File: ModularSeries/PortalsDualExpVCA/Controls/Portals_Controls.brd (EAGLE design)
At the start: 48.5 x 98 mm, 15 parts, among them SW1 SPDT_SWITCHDW1, SW2 SPDT_SWITCHDW1

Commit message: DRC check fixes on Prism, Portals, TimeSeeds and Knives
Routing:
- net AGND: track 142.0 -> 141.3 mm
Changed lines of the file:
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@@
 <wire x1="33" y1="56.7" x2="33.02" y2="57.785" width="0.6096" layer="1"/>
 <wire x1="33.02" y1="57.785" x2="33" y2="65.3" width="0.6096" layer="1" curve="2.417014"/>
-<wire x1="33" y1="65.3" x2="33.02" y2="66.04" width="0.6096" layer="1"/>
 <contactref element="R2" pad="LUGR"/>
 <wire x1="33" y1="65.3" x2="33.02" y2="66.675" width="0.6096" layer="1"/>

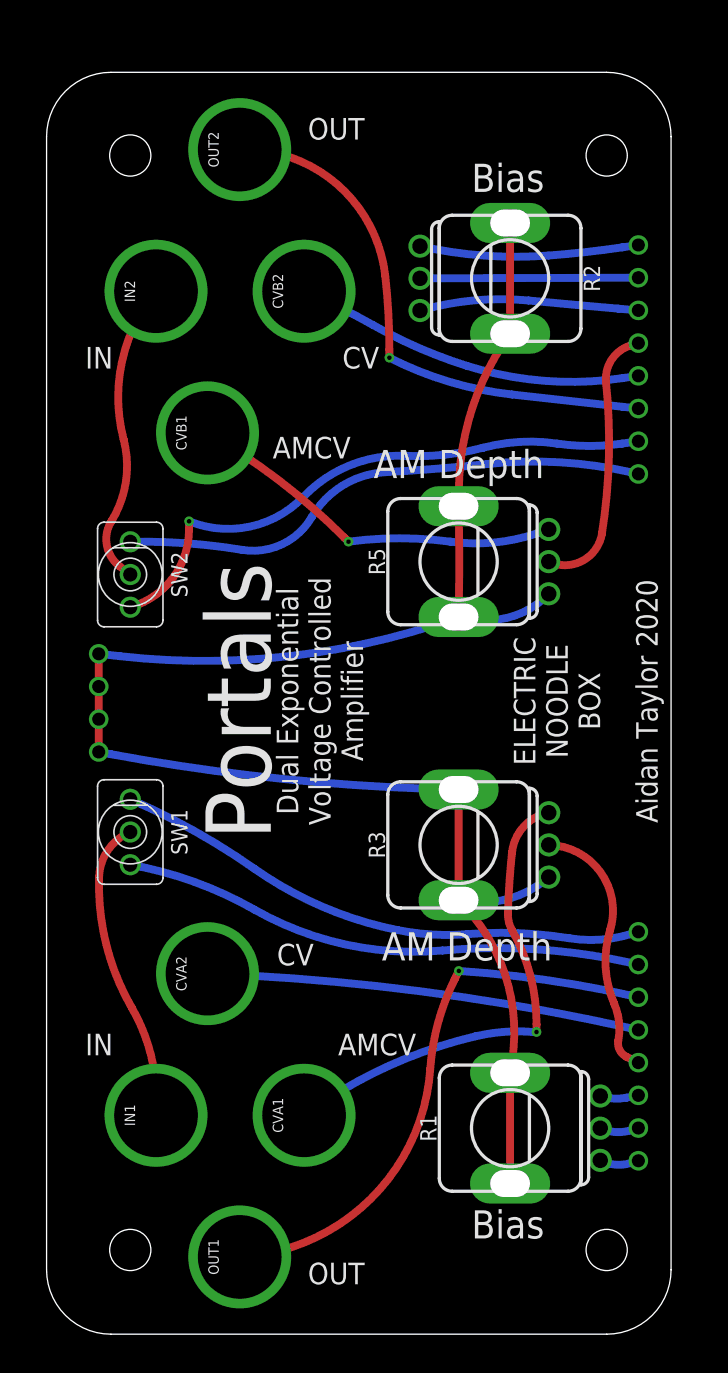
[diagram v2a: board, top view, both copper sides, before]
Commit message: Pulse output fixed on Knives, schematics and layout updated. Panel added for Portals
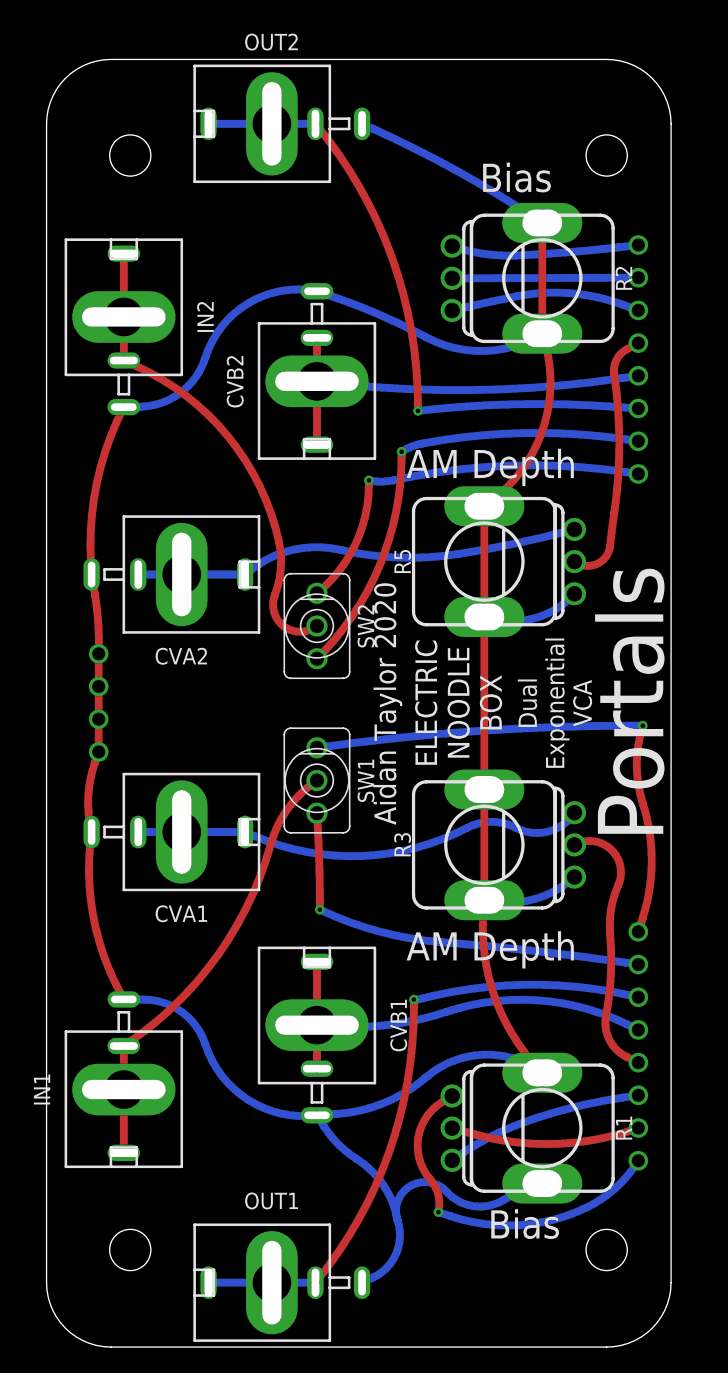
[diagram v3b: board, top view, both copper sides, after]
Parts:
- CVA1, CVA2, CVB1, CVB2, IN1, IN2, OUT1, OUT2: value BANANA_PANEL -> COMBI-JACKCINCHNANA; device ElectricNoodleBox:BANANA_PANEL -> ElectricNoodleBox:NEWCOMBOJACK_PANEL
- moved CVB1 46.8 mm to (22.0, 25.0)
- moved CVA2 31.1 mm to (11.5, 60.0), turned to 270 degrees
- moved CVA1 24.0 mm to (11.5, 40.0), turned to 270 degrees
- moved SW1 15.0 mm to (22.0, 44.0)
- moved SW2 15.0 mm to (22.0, 56.0)
- moved CVB2 7.07 mm to (22.0, 75.0), turned to 180 degrees
- moved IN1 3.20 mm to (7.00, 20.0), turned to 180 degrees
- moved IN2 3.20 mm to (7.00, 80.0)
- moved OUT1 3.20 mm to (18.5, 5.00), turned to 90 degrees
- moved OUT2 3.20 mm to (18.5, 95.0), turned to 90 degrees
- moved R1 2.50 mm to (39.5, 17.0), turned to 270 degrees
- moved R2 2.50 mm to (39.5, 83.0)
- moved R3 2.00 mm to (35.0, 39.0)
- moved R5 2.00 mm to (35.0, 61.0)
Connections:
- net AGND: now also CVA1.S, CVA2.S, CVB1.S, CVB2.S, IN1.S, IN2.S, OUT1.S, OUT2.S
- net N$1: now also CVB1.CONN, CVB1.T1, CVB1.T2; no longer CVA2.CONN
- net N$11: now also CVA2.CONN, CVA2.T1, CVA2.T2; no longer CVB1.CONN
- net N$19: now also OUT2.T1, OUT2.T2
- net N$2: now also CVB2.T1, CVB2.T2
- net N$22: now also IN2.T1, IN2.T2
- net N$3: now also CVA1.T1, CVA1.T2
- net N$8: now also OUT1.T1, OUT1.T2
- net N$9: now also IN1.T1, IN1.T2
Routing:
- net AGND: track 141.3 -> 244.9 mm
- net N$6: track 3.00 -> 26.6 mm, vias 0 -> 1
- net N$7: track 2.98 -> 15.4 mm
- net N$22: track 22.8 -> 35.1 mm
- net N$5: track 2.99 -> 14.5 mm
- net N$9: track 23.3 -> 33.8 mm
- net N$21: track 41.1 -> 30.6 mm, vias 0 -> 1
- net N$20: track 44.0 -> 35.9 mm
- net N$19: track 41.1 -> 49.1 mm
- net N$10: track 40.5 -> 32.7 mm, vias 0 -> 1
- net N$8: track 42.8 -> 49.1 mm
- net N$2: track 27.3 -> 33.3 mm
- net N$11: track 29.5 -> 34.4 mm, vias 1 -> 0
- net N$3: track 37.9 -> 34.1 mm, vias 1 -> 0
- net N$16: track 17.0 -> 14.5 mm
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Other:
- board size 48.5 x 98 mm -> 48.5 x 100 mm
- board text added: "Dual Exponential VCA"
- board text removed: "AMCV"
- board text removed: "CV"
- board text removed: "Dual Exponential Voltage Controlled Amplifier"
- board text removed: "IN"
- board text removed: "OUT"

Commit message: Panel for TimeSeeds added. TLHP core PCB added
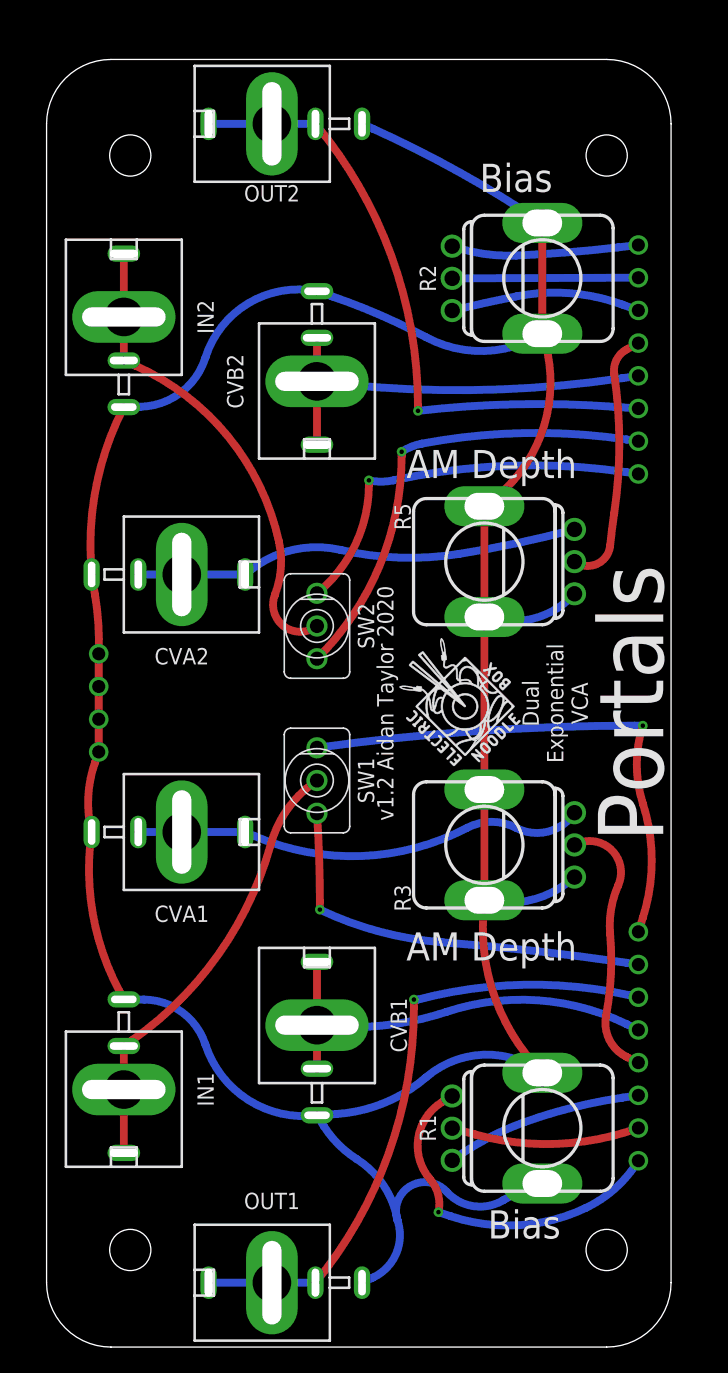
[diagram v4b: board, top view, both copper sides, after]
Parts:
- added U$1, U$2: (no value), ElectricNoodleBox:LOGO10X10
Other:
- board text added: "v1.2 Aidan Taylor 2020"
- board text removed: "Aidan Taylor 2020"
- board text removed: "ELECTRIC NOODLE BOX"
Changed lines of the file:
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@@
 <?xml version="1.0" encoding="utf-8"?>
 <!DOCTYPE eagle SYSTEM "eagle.dtd">
-<eagle version="9.6.0">
+<eagle version="9.6.2">
 <drawing>
 <settings>
@@
 <layer number="17" name="Pads" color="2" fill="1" visible="yes" active="yes"/>
 <layer number="18" name="Vias" color="2" fill="1" visible="yes" active="yes"/>
-<layer number="19" name="Unrouted" color="6" fill="1" visible="yes" active="yes"/>
+<layer number="19" name="Unrouted" color="6" fill="1" visible="no" active="yes"/>
 <layer number="20" name="Dimension" color="24" fill="1" visible="yes" active="yes"/>
 <layer number="21" name="tPlace" color="7" fill="1" visible="yes" active="yes"/>
 <layer number="22" name="bPlace" color="7" fill="1" visible="yes" active="yes"/>
-<layer number="23" name="tOrigins" color="15" fill="1" visible="yes" active="yes"/>
-<layer number="24" name="bOrigins" color="15" fill="1" visible="yes" active="yes"/>
+<layer number="23" name="tOrigins" color="15" fill="1" visible="no" active="yes"/>
+<layer number="24" name="bOrigins" color="15" fill="1" visible="no" active="yes"/>
 <layer number="25" name="tNames" color="7" fill="1" visible="yes" active="yes"/>
-<layer number="26" name="bNames" color="7" fill="1" visible="yes" active="yes"/>
+<layer number="26" name="bNames" color="7" fill="1" visible="no" active="yes"/>
 <layer number="27" name="tValues" color="7" fill="1" visible="no" active="yes"/>
 <layer number="28" name="bValues" color="7" fill="1" visible="no" active="yes"/>
@@
 <layer number="37" name="tTest" color="7" fill="1" visible="no" active="yes"/>
 <layer number="38" name="bTest" color="7" fill="1" visible="no" active="yes"/>
-<layer number="39" name="tKeepout" color="4" fill="11" visible="yes" active="yes"/>
-<layer number="40" name="bKeepout" color="1" fill="11" visible="yes" active="yes"/>
-<layer number="41" name="tRestrict" color="4" fill="10" visible="yes" active="yes"/>
-<layer number="42" name="bRestrict" color="1" fill="10" visible="yes" active="yes"/>
-<layer number="43" name="vRestrict" color="2" fill="10" visible="yes" active="yes"/>
+<layer number="39" name="tKeepout" color="4" fill="11" visible="no" active="yes"/>
+<layer number="40" name="bKeepout" color="1" fill="11" visible="no" active="yes"/>
+<layer number="41" name="tRestrict" color="4" fill="10" visible="no" active="yes"/>
+<layer number="42" name="bRestrict" color="1" fill="10" visible="no" active="yes"/>
+<layer number="43" name="vRestrict" color="2" fill="10" visible="no" active="yes"/>
 <layer number="44" name="Drills" color="7" fill="1" visible="no" active="yes"/>
 <layer number="45" name="Holes" color="7" fill="1" visible="no" active="yes"/>
-<layer number="46" name="Milling" color="3" fill="1" visible="no" active="yes"/>
+<layer number="46" name="Milling" color="3" fill="1" visible="yes" active="yes"/>
 <layer number="47" name="Measures" color="7" fill="1" visible="no" active="yes"/>
-<layer number="48" name="Document" color="7" fill="1" visible="yes" active="yes"/>
+<layer number="48" name="Document" color="7" fill="1" visible="no" active="yes"/>
 <layer number="49" name="Reference" color="7" fill="1" visible="yes" active="yes"/>
 <layer number="50" name="dxf" color="7" fill="1" visible="no" active="no"/>
-<layer number="51" name="tDocu" color="7" fill="1" visible="yes" active="yes"/>
-<layer number="52" name="bDocu" color="7" fill="1" visible="yes" active="yes"/>
+<layer number="51" name="tDocu" color="7" fill="1" visible="no" active="yes"/>
+<layer number="52" name="bDocu" color="7" fill="1" visible="no" active="yes"/>
 <layer number="53" name="tGND_GNDA" color="7" fill="9" visible="no" active="no"/>
 <layer number="54" name="bGND_GNDA" color="1" fill="9" visible="no" active="no"/>
@@
 </layers>
 <board>
-<fusionsync huburn="a.cGVyc29uYWw6dWUyYjdlNGE0" projecturn="a.cGVyc29uYWw6dWUyYjdlNGE0IzIwMjAwNDA1MjgzMzA0MTgx" f3durn="urn:adsk.wipprod:dm.lineage:XfjEGdqqSi-9eQBJwCMZSQ" pcbguid="25871f84-74d5-4f7c-8471-5e8c6ea129c0" lastpulledtime="" lastsyncedchangeguid="" latestrevisionid="99b6558b-c879-43a6-8e26-3714c5e8d2b9" lastsyncedrevisionid="99b6558b-c879-43a6-8e26-3714c5e8d2b9" lastboardhashguid="6312c004-2ac3-f14a-2101-901f34501693" lastpushedtime="2020-05-26T18:30:07Z" linktopcb3d="%12"/>
+<fusionsync huburn="a.cGVyc29uYWw6dWUyYjdlNGE0" projecturn="a.cGVyc29uYWw6dWUyYjdlNGE0IzIwMjAwNDA1MjgzMzA0MTgx" f3durn="urn:adsk.wipprod:dm.lineage:XfjEGdqqSi-9eQBJwCMZSQ" pcbguid="" lastpulledtime="" lastsyncedchangeguid="" latestrevisionid="d212331a-2d97-479f-80fb-10bf9934a00b" lastsyncedrevisionid="d212331a-2d97-479f-80fb-10bf9934a00b" lastboardhashguid="82df6d0b-af90-7169-ef29-52b558667a44" lastpushedtime="2020-06-25T11:09:44Z" linktopcb3d="true"/>
 <plain>
 <text x="37.465" y="90.805" size="2.1844" layer="21" font="vector" ratio="16" align="center">Bias</text>
@@
 <text x="38.1" y="9.525" size="2.1844" layer="21" font="vector" ratio="16" align="center">Bias</text>
 <text x="46.355" y="50" size="5.08" layer="21" font="vector" ratio="16" rot="R90" align="center">Portals</text>
-<text x="40.5" y="50" size="1.4224" layer="21" font="vector" ratio="16" rot="R90" align="center">Dual
+<text x="40.5" y="50" size="1.27" layer="21" font="vector" ratio="16" rot="R90" align="center">Dual
 Exponential
 VCA</text>
-<text x="33" y="50" size="1.6764" layer="21" font="vector" ratio="16" rot="R90" align="center">ELECTRIC
-NOODLE
-BOX</text>
-<text x="27.305" y="50" size="1.6764" layer="21" font="vector" ratio="16" rot="R90" align="center">Aidan Taylor 2020</text>
+<text x="27.305" y="50" size="1.27" layer="21" font="vector" ratio="16" rot="R90" align="center">v1.2 Aidan Taylor 2020</text>
 <wire x1="0" y1="-14.25" x2="50.5" y2="-14.25" width="0.6096" layer="49"/>
 <wire x1="50.5" y1="-14.25" x2="50.5" y2="-8.25" width="0.6096" layer="49"/>
@@
 <element name="BOARD1" library="ElectricNoodleBox" package="PORTALS" value="PORTALS_LINK" x="49.5" y="2.54" smashed="yes" rot="MR0"/>
 <element name="R1" library="ElectricNoodleBox" package="ALPHA_RV09_9MMPOT" value="100K" x="39.5" y="17" smashed="yes" rot="R270">
-<attribute name="NAME" x="45.85" y="17" size="1.27" layer="25" rot="R270" align="center"/>
+<attribute name="NAME" x="30.61" y="17" size="1.27" layer="25" rot="R270" align="center"/>
 <attribute name="VALUE" x="31.88" y="9.38" size="1.27" layer="27" rot="R270" align="center"/>
 </element>
 <element name="R2" library="ElectricNoodleBox" package="ALPHA_RV09_9MMPOT" value="100K" x="39.5" y="83" smashed="yes" rot="R270">
-<attribute name="NAME" x="45.85" y="83" size="1.27" layer="25" rot="R270" align="center"/>
+<attribute name="NAME" x="30.61" y="83" size="1.27" layer="25" rot="R270" align="center"/>
 <attribute name="VALUE" x="31.88" y="75.38" size="1.27" layer="27" rot="R270" align="center"/>
 </element>
 <element name="R3" library="ElectricNoodleBox" package="ALPHA_RV09_9MMPOT" value="100k" x="35" y="39" smashed="yes" rot="R90">
-<attribute name="NAME" x="28.65" y="39" size="1.27" layer="25" rot="R90" align="center"/>
+<attribute name="NAME" x="28.65" y="34.8725" size="1.27" layer="25" rot="R90" align="center"/>
 <attribute name="VALUE" x="42.62" y="46.62" size="1.27" layer="27" rot="R90" align="center"/>
 </element>
 <element name="R5" library="ElectricNoodleBox" package="ALPHA_RV09_9MMPOT" value="100K" x="35" y="61" smashed="yes" rot="R90">
-<attribute name="NAME" x="28.65" y="61" size="1.27" layer="25" rot="R90" align="center"/>
+<attribute name="NAME" x="28.65" y="64.4925" size="1.27" layer="25" rot="R90" align="center"/>
 <attribute name="VALUE" x="42.62" y="68.62" size="1.27" layer="27" rot="R90" align="center"/>
 </element>
@@
 </element>
 <element name="IN1" library="ElectricNoodleBox" package="NEWCOMBOJACK_PANEL" value="COMBI-JACKCINCHNANA" x="7" y="20" smashed="yes" rot="R180">
-<attribute name="NAME" x="0.65" y="20" size="1.27" layer="25" font="vector" rot="R270" align="center"/>
+<attribute name="NAME" x="13.35" y="20" size="1.27" layer="25" font="vector" rot="R270" align="center"/>
 </element>
 <element name="OUT2" library="ElectricNoodleBox" package="NEWCOMBOJACK_PANEL" value="COMBI-JACKCINCHNANA" x="18.5" y="95" smashed="yes" rot="R90">
-<attribute name="NAME" x="18.5" y="101.35" size="1.27" layer="25" font="vector" rot="R180" align="center"/>
+<attribute name="NAME" x="18.5" y="89.6025" size="1.27" layer="25" font="vector" rot="R180" align="center"/>
 </element>
 <element name="IN2" library="ElectricNoodleBox" package="NEWCOMBOJACK_PANEL" value="COMBI-JACKCINCHNANA" x="7" y="80" smashed="yes">
 <attribute name="NAME" x="13.35" y="80" size="1.27" layer="25" font="vector" rot="R90" align="center"/>
 </element>
+<element name="U$1" library="ElectricNoodleBox" package="LOGO10X10" value="" x="38.1" y="45.085" smashed="yes" rot="R90"/>
+<element name="U$2" library="ElectricNoodleBox" package="LOGO10X10" value="" x="33.9725" y="53.6575" smashed="yes" rot="MR270"/>
 </elements>
 <signals>

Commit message: Layout and schematic renders for LHP added
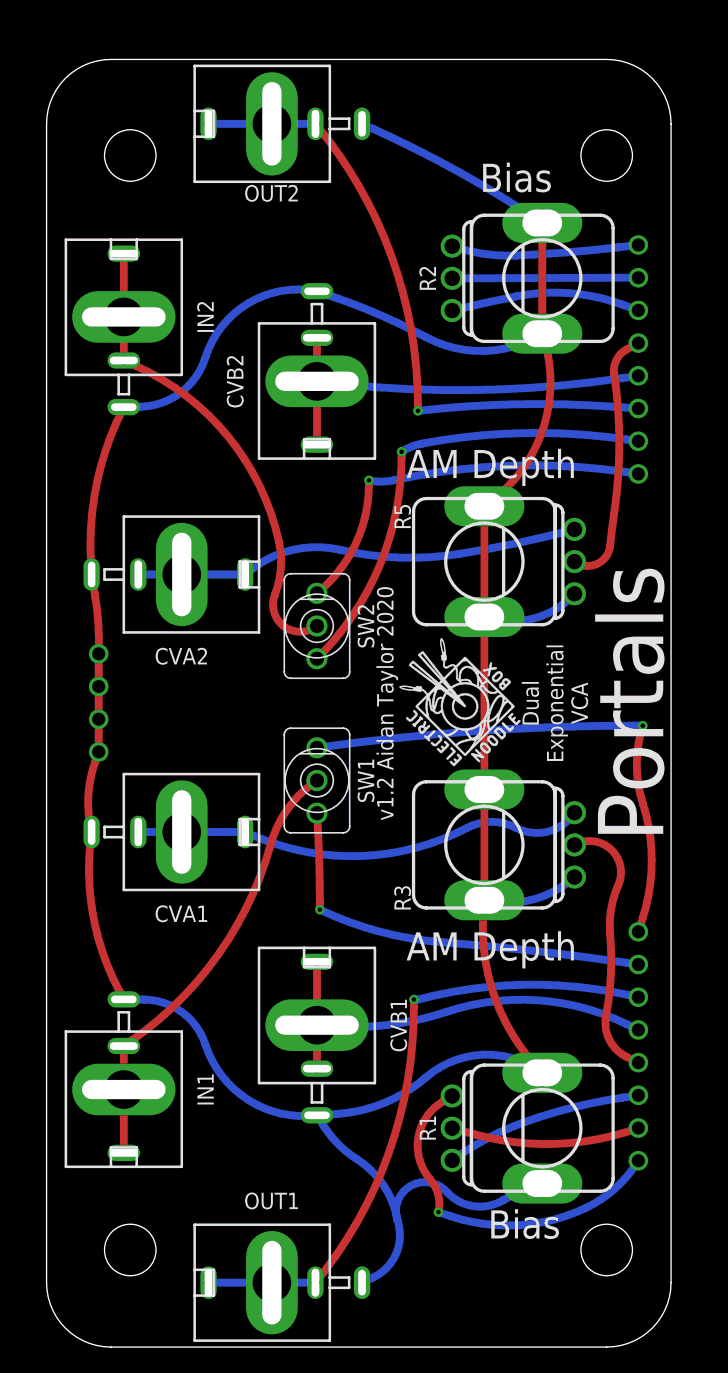
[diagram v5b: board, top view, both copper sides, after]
